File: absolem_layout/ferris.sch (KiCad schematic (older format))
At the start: 109 parts, among them IC1 NUF2221W1T2G, J1 USB C, K0_0 KEYSW, K0_1 KEYSW, K0_2 KEYSW, K0_3 KEYSW, K0_4 KEYSW, K0_5 KEYSW, K0_6 KEYSW, K0_7 KEYSW, K0_8 KEYSW, K0_9 KEYSW, K1_0 KEYSW, K1_1 KEYSW, K1_2 KEYSW, K1_3 KEYSW, K1_4 KEYSW, K1_5 KEYSW, K1_6 KEYSW, K1_7 KEYSW, K1_8 KEYSW, K1_9 KEYSW, K2_0 KEYSW, K2_1 KEYSW, K2_2 KEYSW, K2_3 KEYSW, K2_4 KEYSW, K2_5 KEYSW, K2_6 KEYSW, K2_7 KEYSW, K2_8 KEYSW, K2_9 KEYSW, K3_2 KEYSW, K3_3 KEYSW, K3_4 KEYSW, K3_5 KEYSW, K3_6 KEYSW, K3_7 KEYSW, SW1 SW_PUSH, SW2 SW_PUSH, U1 ATmega32U4-AU, U2 TLV70012_SOT23-5, U3 STM32F303CBTx, Y1 Crystal, Y2 8MHz

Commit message: More connections, removed line termination resistors (now we use an IC for it!)
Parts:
- removed C1, C2: 22p, Capacitor_SMD:C_0805_2012Metric_Pad1.15x1.40mm_HandSolder, symbol ferris-rescue:C_Small-Device
- removed C3, C4, C5, C6: 0.1u, Capacitor_SMD:C_0805_2012Metric_Pad1.15x1.40mm_HandSolder, symbol ferris-rescue:C_Small-Device
- removed C7: 4.7u, Capacitor_SMD:C_0805_2012Metric_Pad1.15x1.40mm_HandSolder, symbol ferris-rescue:C_Small-Device
- removed C8: 1u, Capacitor_SMD:C_0805_2012Metric_Pad1.15x1.40mm_HandSolder, symbol ferris-rescue:C_Small-Device
- removed R1, R2: 10k, Resistor_SMD:R_0805_2012Metric_Pad1.15x1.40mm_HandSolder, symbol ferris-rescue:R-Device
- removed R3, R4: 22, Resistor_SMD:R_0805_2012Metric_Pad1.15x1.40mm_HandSolder, symbol ferris-rescue:R-Device
- removed SW1: SW_PUSH, Button_Switch_SMD:SW_SPST_B3U-1000P, symbol ferris-rescue:SW_PUSH-keyboard_parts-ferris-rescue
- removed U1: ATmega32U4-AU, Package_QFP:TQFP-44_10x10mm_P0.8mm, symbol ferris-rescue:ATmega32U4-AU-MCU_Microchip_ATmega
- removed Y1: Crystal, Crystal:Crystal_SMD_3225-4Pin_3.2x2.5mm, symbol ferris-rescue:Crystal_GND24_Small-Device
- added J2: Conn_01x05_Male, Connector_PinHeader_2.54mm:PinHeader_1x05_P2.54mm_Vertical, symbol Connector:Conn_01x05_Male
- gave numbers to parts that had none: 6
- renumbered C9 to C1, C12 to C10, C13 to C11, C10 to C2, C11 to C6, D0_0 to D0_1, D0_9 to D0_10, D0_1 to D0_2, D0_2 to D0_3, D0_3 to D0_4, D0_4 to D0_5, D0_5 to D0_6, D0_6 to D0_7, D0_7 to D0_8, D0_8 to D0_9, D1_0 to D1_1, D1_9 to D1_10, D1_1 to D1_2, D1_2 to D1_3, D1_3 to D1_4, D1_4 to D1_5, D1_5 to D1_6, D1_6 to D1_7, D1_7 to D1_8, D1_8 to D1_9, D2_0 to D2_1, D2_9 to D2_10, D2_1 to D2_2, D2_2 to D2_3, D2_3 to D2_4, D2_4 to D2_5, D2_5 to D2_6, D2_6 to D2_7, D2_7 to D2_8, D2_8 to D2_9, D3_2 to D3_1, D3_3 to D3_2, D3_4 to D3_3, D3_5 to D3_4, D3_6 to D3_5, D3_7 to D3_6, K0_0 to K0_1, K0_9 to K0_10, K0_1 to K0_2, K0_2 to K0_3, K0_3 to K0_4, K0_4 to K0_5, K0_5 to K0_6, K0_6 to K0_7, K0_7 to K0_8, K0_8 to K0_9, K1_0 to K1_1, K1_9 to K1_10, K1_1 to K1_2, K1_2 to K1_3, K1_3 to K1_4, K1_4 to K1_5, K1_5 to K1_6, K1_6 to K1_7, K1_7 to K1_8, K1_8 to K1_9, K2_0 to K2_1, K2_9 to K2_10, K2_1 to K2_2, K2_2 to K2_3, K2_3 to K2_4, K2_4 to K2_5, K2_5 to K2_6, K2_6 to K2_7, K2_7 to K2_8, K2_8 to K2_9, K3_2 to K3_1, K3_3 to K3_2, K3_4 to K3_3, K3_5 to K3_4, K3_6 to K3_5, K3_7 to K3_6, R5 to R1, R6 to R2, R7 to R5, SW2 to SW1, U2 to U1, U3 to U2, Y2 to Y1
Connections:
- net +3V3: now also J2.5 (Pin_5)
- net D+I: now also J1.A6 (D+), J1.B6 (D+)
- net D-I: now also J1.A7 (D-), J1.B7 (D-)
- net GND: now also J2.2 (Pin_2)
- net col0: now also U2.30 (PA9)
- net col1: now also U2.29 (PA8)
- net col2: now also U2.28 (PB15)
- net col3: now also U2.27 (PB14)
- net col4: now also U2.26 (PB13)
- net col5: now also U2.31 (PA10)
- net col6: now also U2.46 (PB9)
- net col7: now also U2.42 (PB6)
- net col8: now also U2.41 (PB5)
- net col9: now also U2.40 (PB4)
- net row0: now also U2.16 (PA6)
- net row1: now also U2.15 (PA5)
- net row2: now also U2.14 (PA4)
- net row3: now also U2.13 (PA3)
- net LAYER_LED: now reaches D1.4 (DIN)
- net SWD_IO: now reaches U2.34 (PA13)
- net SWD_IO: now also J2.1 (Pin_1)
- net SWCLK: now reaches U2.37 (PA14)
- net SWCLK: now also J2.3 (Pin_3)
- net NRST: now reaches C11.1, U2.7 (NRST)
- net NRST: now also J2.4 (Pin_4)
- no-connect marks 16 -> 3

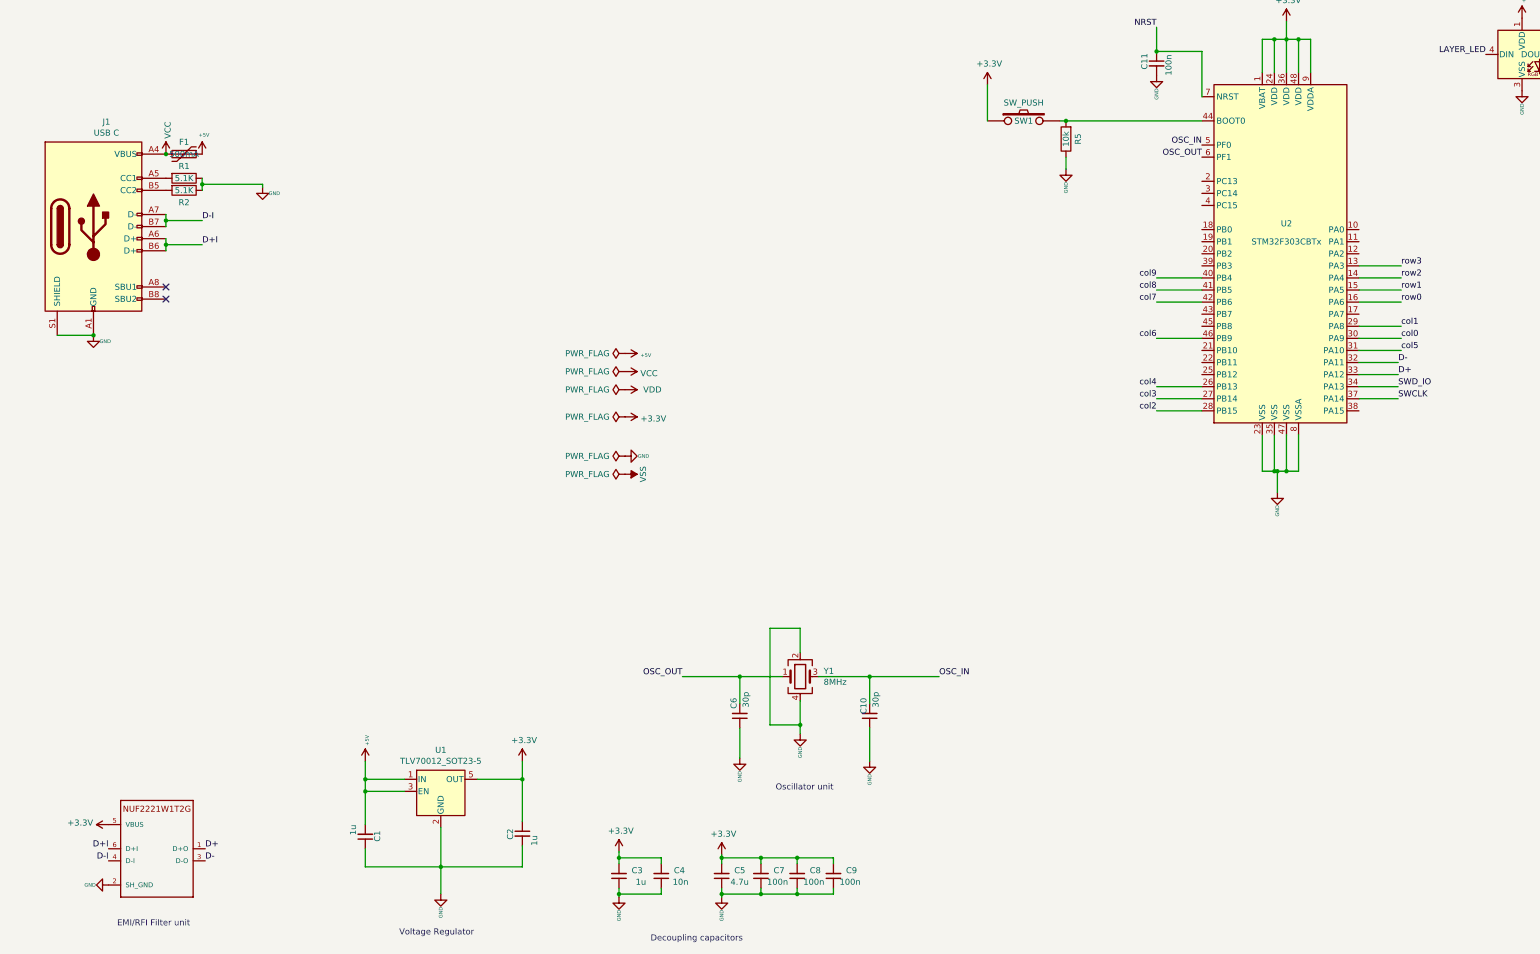
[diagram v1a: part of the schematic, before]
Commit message: Connected up most of the power. PCB incomplete still
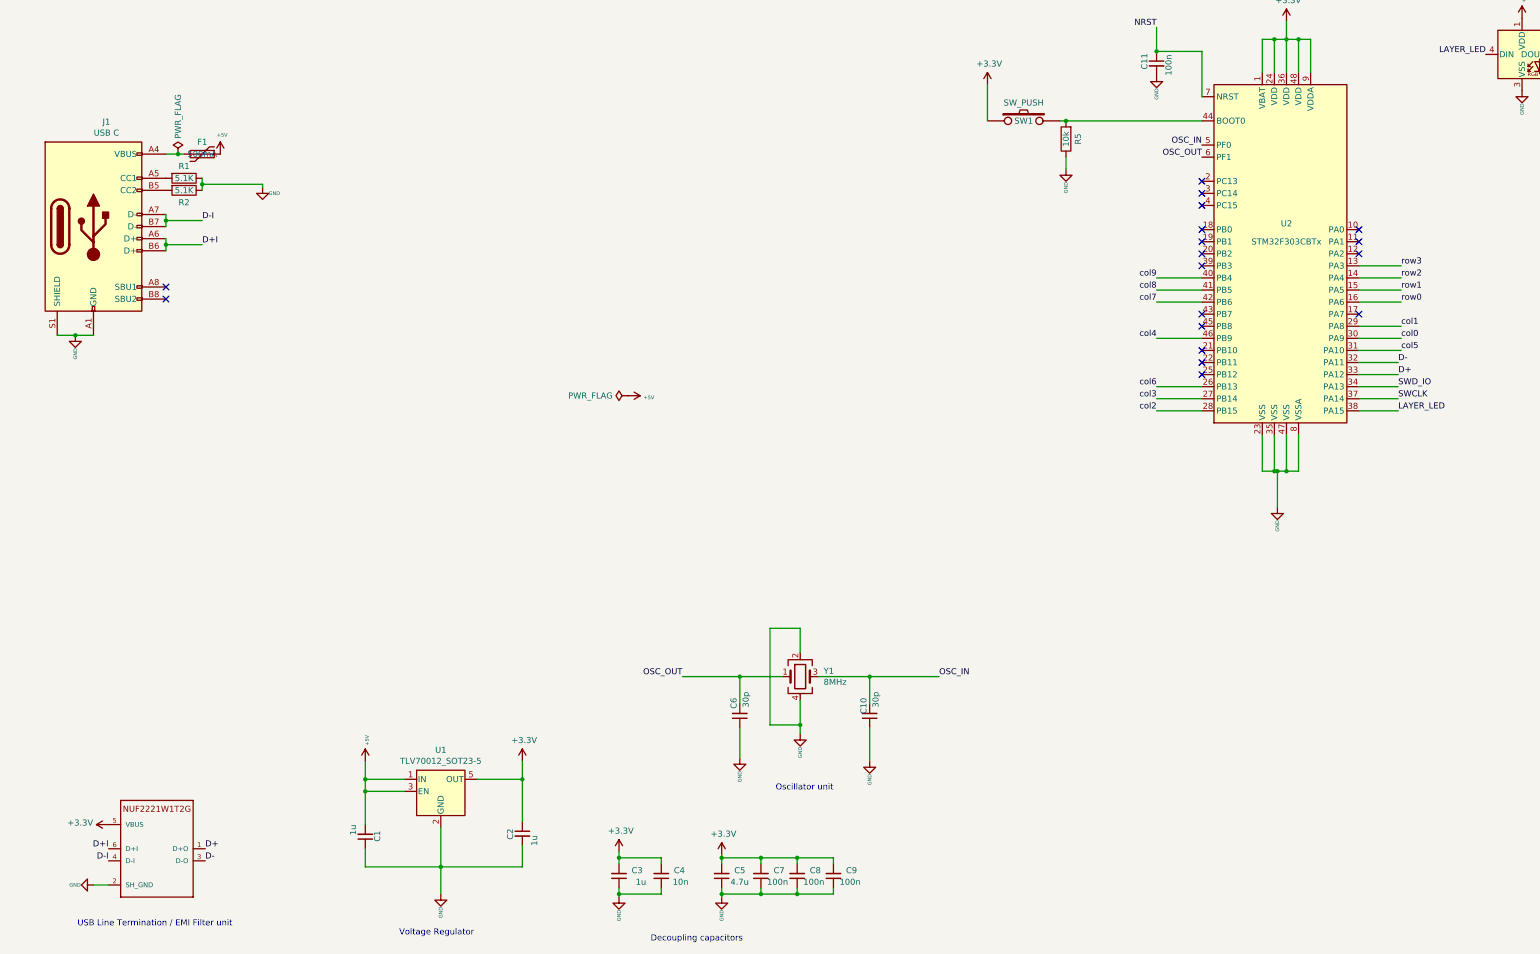
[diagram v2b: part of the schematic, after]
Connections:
- net LAYER_LED: now also U2.38 (PA15)
- net col4: now also U2.46 (PB9); no longer U2.26 (PB13)
- net col6: now also U2.26 (PB13); no longer U2.46 (PB9)
- net VCC: no longer names the net of F1.2, J1.A4 (VBUS), J1.A9 (VBUS), J1.B4 (VBUS), J1.B9 (VBUS)
- no-connect marks 3 -> 19
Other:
- note added: "USB Line Termination / EMI Filter unit"
- note removed: "EMI/RFI Filter unit"
- moved on the sheet: F1

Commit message: Updated the routing and positons
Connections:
- net col0: now also U2.41 (PB5); no longer U2.30 (PA9)
- net col1: now also U2.40 (PB4); no longer U2.29 (PA8)
- net col2: now also U2.42 (PB6); no longer U2.28 (PB15)
- net col3: now also U2.43 (PB7); no longer U2.27 (PB14)
- net col5: now also U2.14 (PA4); no longer U2.31 (PA10)
- net col6: now also U2.15 (PA5); no longer U2.26 (PB13)
- net col7: now also U2.16 (PA6); no longer U2.42 (PB6)
- net col8: now also U2.28 (PB15); no longer U2.41 (PB5)
- net col9: now also U2.27 (PB14); no longer U2.40 (PB4)
- net row0: now also U2.31 (PA10); no longer U2.16 (PA6)
- net row1: now also U2.30 (PA9); no longer U2.15 (PA5)
- net row2: now also U2.29 (PA8); no longer U2.14 (PA4)
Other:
- note added: "USB Connection"
- moved on the sheet: F1, J1, R1, R2
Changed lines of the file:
@@
 L ferris-rescue:R-Device R1
 U 1 1 5ED68FE1
-P 1700 4800
-F 0 "R1" V 1600 4800 50  0000 C CNN
-F 1 "5.1K" V 1700 4800 50  0000 C CNN
-F 2 "Resistor_SMD:R_0805_2012Metric_Pad1.15x1.40mm_HandSolder" V 1630 4800 50  0001 C CNN
-F 3 "~" H 1700 4800 50  0001 C CNN
-F 4 "C27834" V 1700 4800 50  0001 C CNN "LCSC Part #"
-	1    1700 4800
+P 2550 4975
+F 0 "R1" V 2450 4975 50  0000 C CNN
+F 1 "5.1K" V 2550 4975 50  0000 C CNN
+F 2 "Resistor_SMD:R_0805_2012Metric_Pad1.15x1.40mm_HandSolder" V 2480 4975 50  0001 C CNN
+F 3 "~" H 2550 4975 50  0001 C CNN
+F 4 "C27834" V 2550 4975 50  0001 C CNN "LCSC Part #"
+	1    2550 4975
 	0    1    1    0
 $EndComp
@@
 L ferris-rescue:R-Device R2
 U 1 1 5ED69FD6
-P 1700 4900
-F 0 "R2" V 1800 4900 50  0000 C CNN
-F 1 "5.1K" V 1700 4900 50  0000 C CNN
-F 2 "Resistor_SMD:R_0805_2012Metric_Pad1.15x1.40mm_HandSolder" V 1630 4900 50  0001 C CNN
-F 3 "~" H 1700 4900 50  0001 C CNN
-	1    1700 4900
+P 2550 5075
+F 0 "R2" V 2650 5075 50  0000 C CNN
+F 1 "5.1K" V 2550 5075 50  0000 C CNN
+F 2 "Resistor_SMD:R_0805_2012Metric_Pad1.15x1.40mm_HandSolder" V 2480 5075 50  0001 C CNN
+F 3 "~" H 2550 5075 50  0001 C CNN
+	1    2550 5075
 	0    1    1    0
 $EndComp
@@
 L power:GND #PWR06
 U 1 1 5ED72D47
-P 2350 4875
-F 0 "#PWR06" H 2350 4925 20  0001 C CNN
-F 1 "GND" H 2400 4825 30  0000 L CNN
-F 2 "" H 2350 4875 60  0000 C CNN
-F 3 "" H 2350 4875 60  0000 C CNN
-	1    2350 4875
-	1    0    0    -1
-$EndComp
-Wire Wire Line
-	1550 5400 1550 5350
-Wire Wire Line
-	1550 5200 1550 5150
+P 3200 5050
+F 0 "#PWR06" H 3200 5100 20  0001 C CNN
+F 1 "GND" H 3250 5000 30  0000 L CNN
+F 2 "" H 3200 5050 60  0000 C CNN
+F 3 "" H 3200 5050 60  0000 C CNN
+	1    3200 5050
+	1    0    0    -1
+$EndComp
+Wire Wire Line
+	2400 5575 2400 5525
+Wire Wire Line
+	2400 5375 2400 5325
 $Comp
 L ferris-rescue:USB_C_Receptacle_USB2.0-Connector J1
 U 1 1 5EF5D00C
-P 950 5200
-F 0 "J1" H 1057 6067 50  0000 C CNN
-F 1 "USB C" H 1057 5976 50  0000 C CNN
-F 2 "Connector_USB:USB_C_Receptacle_HRO_TYPE-C-31-M-12" H 1100 5200 50  0001 C CNN
-F 3 "https://www.usb.org/sites/default/files/documents/usb_type-c.zip" H 1100 5200 50  0001 C CNN
-F 4 "C165948" H 950 5200 50  0001 C CNN "LCSC Part #"
-	1    950  5200
+P 1800 5375
+F 0 "J1" H 1907 6242 50  0000 C CNN
+F 1 "USB C" H 1907 6151 50  0000 C CNN
+F 2 "Connector_USB:USB_C_Receptacle_HRO_TYPE-C-31-M-12" H 1950 5375 50  0001 C CNN
+F 3 "https://www.usb.org/sites/default/files/documents/usb_type-c.zip" H 1950 5375 50  0001 C CNN
+F 4 "C165948" H 1800 5375 50  0001 C CNN "LCSC Part #"
+	1    1800 5375
 	1    0    0    -1
 $EndComp
@@
 Wire Wire Line
 	7750 900  7750 1200
-Text Label 15200 875  2    50   ~ 0
-row1,0
-Text Label 15200 1000 2    50   ~ 0
-row1,1
 $Comp
 L ferris-rescue:KEYSW-keyboard_parts-ferris-rescue K1_6
@@
 	1    0    0    -1
 $EndComp
-Text Label 15200 1125 2    50   ~ 0
-row1,2
 $Comp
 L ferris-rescue:D-Device D2_6
@@
 Wire Wire Line
 	8550 2700 9250 2700
-NoConn ~ 1550 5700
-NoConn ~ 1550 5800
+NoConn ~ 2400 5875
+NoConn ~ 2400 5975
 Wire Wire Line
 	10550 1800 10550 2400
@@
 Connection ~ 7750 2400
 Connection ~ 7150 3300
-Text Label 1850 5350 0    50   ~ 0
+Text Label 2700 5525 0    50   ~ 0
 D+I
-Text Label 1850 5150 0    50   ~ 0
+Text Label 2700 5325 0    50   ~ 0
 D-I
 $Comp
 L ferris-rescue:Polyfuse-Device F1
 U 1 1 5EF6C20F
-P 1850 4600
-F 0 "F1" V 1750 4600 50  0000 C CNN
-F 1 "500mA" V 1850 4600 50  0000 C CNN
-F 2 "Fuse:Fuse_1206_3216Metric" H 1900 4400 50  0001 L CNN
-F 3 "~" H 1850 4600 50  0001 C CNN
-F 4 "C151162" V 1850 4600 50  0001 C CNN "LCSC Part #"
-	1    1850 4600
+P 2700 4775
+F 0 "F1" V 2600 4775 50  0000 C CNN
+F 1 "500mA" V 2700 4775 50  0000 C CNN
+F 2 "Fuse:Fuse_1206_3216Metric" H 2750 4575 50  0001 L CNN
+F 3 "~" H 2700 4775 50  0001 C CNN
+F 4 "C151162" V 2700 4775 50  0001 C CNN "LCSC Part #"
+	1    2700 4775
 	0    1    1    0
 $EndComp
@@
 L ferris-rescue:+5V-power #PWR05
 U 1 1 5EF7A4D9
-P 2000 4600
-F 0 "#PWR05" H 2000 4570 20  0001 C CNN
-F 1 "+5V" H 2015 4758 30  0000 C CNN
-F 2 "" H 2000 4600 60  0000 C CNN
-F 3 "" H 2000 4600 60  0000 C CNN
-	1    2000 4600
-	1    0    0    -1
-$EndComp
-Wire Wire Line
-	1850 4800 1850 4850
-Wire Wire Line
-	650  6100 800  6100
+P 2850 4775
+F 0 "#PWR05" H 2850 4745 20  0001 C CNN
+F 1 "+5V" H 2865 4933 30  0000 C CNN
+F 2 "" H 2850 4775 60  0000 C CNN
+F 3 "" H 2850 4775 60  0000 C CNN
+	1    2850 4775
+	1    0    0    -1
+$EndComp
+Wire Wire Line
+	2700 4975 2700 5025
+Wire Wire Line
+	1500 6275 1650 6275
 $Comp
 L ferris-rescue:+5V-power #PWR012
@@
 	7850 3300 8550 3300
 Connection ~ 7850 3300
-Text Label 15200 1250 2    50   ~ 0
-row1,3
 Wire Wire Line
 	3850 2700 7150 2700
@@
 Connection ~ 4450 2400
 NoConn ~ 13075 3775
-Text Label 15500 1250 0    50   ~ 0
-row1,3
-Text Label 15525 1100 0    50   ~ 0
-row1,2
-Text Label 15500 975  0    50   ~ 0
-row1,1
-Text Label 15525 850  0    50   ~ 0
-row1,0
 $Comp
 L NUF2221W1T2G:NUF2221W1T2G IC1
@@
 Wire Wire Line
 	11425 5825 11775 5825
-Text Label 11775 5625 0    50   ~ 0
+Text Label 11775 6025 0    50   ~ 0
 row2
-Text Label 11775 5725 0    50   ~ 0
+Text Label 11775 6125 0    50   ~ 0
 row1
+Text Label 11775 6225 0    50   ~ 0
+row0
+Wire Wire Line
+	11425 6025 11775 6025
+Wire Wire Line
+	11425 6125 11775 6125
+Wire Wire Line
+	11425 6225 11775 6225
 Text Label 11775 5825 0    50   ~ 0
-row0
-Wire Wire Line
-	11425 6025 11775 6025
-Wire Wire Line
-	11425 6125 11775 6125
-Wire Wire Line
-	11425 6225 11775 6225
-Text Label 11775 6025 0    50   ~ 0
-col1
-Text Label 11775 6125 0    50   ~ 0
+col7
+Text Label 9750 5725 2    50   ~ 0
 col0
-Text Label 11775 6225 0    50   ~ 0
-col5
 $Comp
 L ferris-rescue:WS2812B-LED D1
@@
 Text Label 12475 3775 2    50   ~ 0
 LAYER_LED
-Text Label 9750 6725 2    50   ~ 0
-col2
 Wire Wire Line
 	9750 6725 10125 6725
@@
 	10125 6625 9750 6625
 Wire Wire Line
-	10125 6525 9750 6525
-Wire Wire Line
 	10125 6125 9750 6125
-Text Label 9750 6625 2    50   ~ 0
-col3
 Text Label 9750 6125 2    50   ~ 0
 col4
-Text Label 9750 6525 2    50   ~ 0
+Text Label 11775 5725 0    50   ~ 0
 col6
-Text Label 9750 5825 2    50   ~ 0
-col7
+Text Label 9750 5625 2    50   ~ 0
+col1
 Wire Wire Line
 	9750 5825 10125 5825
@@
 Wire Wire Line
 	10125 5625 9750 5625
-Text Label 9750 5725 2    50   ~ 0
+Text Label 9750 6725 2    50   ~ 0
 col8
-Text Label 9750 5625 2    50   ~ 0
+Text Label 9750 6625 2    50   ~ 0
 col9
 Text Label 9750 3550 2    50   ~ 0
@@
 	11750 6625 11425 6625
 Wire Wire Line
-	1550 5150 1850 5150
-Connection ~ 1550 5150
-Wire Wire Line
-	1550 5150 1550 5100
-Wire Wire Line
-	1850 5350 1550 5350
-Connection ~ 1550 5350
-Wire Wire Line
-	1550 5350 1550 5300
-Wire Wire Line
-	1850 4850 2350 4850
-Wire Wire Line
-	2350 4850 2350 4875
-Connection ~ 1850 4850
-Wire Wire Line
-	1850 4850 1850 4900
+	2400 5325 2700 5325
+Connection ~ 2400 5325
+Wire Wire Line
+	2400 5325 2400 5275
+Wire Wire Line
+	2700 5525 2400 5525
+Connection ~ 2400 5525
+Wire Wire Line
+	2400 5525 2400 5475
+Wire Wire Line
+	2700 5025 3200 5025
+Wire Wire Line
+	3200 5025 3200 5050
+Connection ~ 2700 5025
+Wire Wire Line
+	2700 5025 2700 5075
 NoConn ~ 10125 4825
 NoConn ~ 10125 4925
@@
 NoConn ~ 10125 6325
 NoConn ~ 10125 6225
-NoConn ~ 10125 5925
 NoConn ~ 10125 6025
 NoConn ~ 10125 5325
@@
 L power:GND #PWR0101
 U 1 1 5F8C4642
-P 800 6100
-F 0 "#PWR0101" H 800 6150 20  0001 C CNN
-F 1 "GND" V 800 5900 30  0000 L CNN
-F 2 "" H 800 6100 60  0000 C CNN
-F 3 "" H 800 6100 60  0000 C CNN
-	1    800  6100
-	1    0    0    -1
-$EndComp
-Connection ~ 800  6100
-Wire Wire Line
-	800  6100 950  6100
+P 1650 6275
+F 0 "#PWR0101" H 1650 6325 20  0001 C CNN
+F 1 "GND" V 1650 6075 30  0000 L CNN
+F 2 "" H 1650 6275 60  0000 C CNN
+F 3 "" H 1650 6275 60  0000 C CNN
+	1    1650 6275
+	1    0    0    -1
+$EndComp
+Connection ~ 1650 6275
+Wire Wire Line
+	1650 6275 1800 6275
 $Comp
 L power:GND #PWR0102
@@
 $EndComp
 Wire Wire Line
-	1700 4600 1650 4600
+	2550 4775 2500 4775
 Wire Wire Line
 	1075 10650 950  10650
@@
 L ferris-rescue:PWR_FLAG-power #FLG0102
 U 1 1 5F962B5E
-P 1650 4600
-F 0 "#FLG0102" H 1650 4675 50  0001 C CNN
-F 1 "PWR_FLAG" V 1650 4727 50  0000 L CNN
-F 2 "" H 1650 4600 50  0001 C CNN
-F 3 "~" H 1650 4600 50  0001 C CNN
-	1    1650 4600
-	1    0    0    -1
-$EndComp
-Connection ~ 1650 4600
-Wire Wire Line
-	1650 4600 1550 4600
+P 2500 4775
+F 0 "#FLG0102" H 2500 4850 50  0001 C CNN
+F 1 "PWR_FLAG" V 2500 4902 50  0000 L CNN
+F 2 "" H 2500 4775 50  0001 C CNN
+F 3 "~" H 2500 4775 50  0001 C CNN
+	1    2500 4775
+	1    0    0    -1
+$EndComp
+Connection ~ 2500 4775
+Wire Wire Line
+	2500 4775 2400 4775
 Text Label 11750 6725 0    50   ~ 0
 LAYER_LED
 Wire Wire Line
 	11750 6725 11425 6725
+Wire Wire Line
+	10125 5925 9750 5925
+Text Label 9750 5825 2    50   ~ 0
+col2
+Text Label 9750 5925 2    50   ~ 0
+col3
+Text Label 11775 5625 0    50   ~ 0
+col5
+NoConn ~ 10125 6525
+Text Notes 2025 6650 2    50   ~ 0
+USB Connection
 $EndSCHEMATC

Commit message: Prefinal version
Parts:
- removed J2: Conn_01x05_Male, Connector_PinHeader_2.54mm:PinHeader_1x05_P2.54mm_Vertical, symbol Connector:Conn_01x05_Male
- added C12: 10uF, Capacitor_SMD:C_0805_2012Metric_Pad1.15x1.40mm_HandSolder, symbol ferris-rescue:C_Small-Device
- added D1_11: D, Diode_SMD:D_SOD-123, symbol ferris-rescue:D-Device
- added Q1: DTC123J, Package_TO_SOT_SMD:SOT-23, symbol Transistor_BJT:DTC123J
- C11: value 100n -> 4.7nF
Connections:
- net GND: now also C12.2, Q1.2 (E)
- net at R5.2, U2.44 (BOOT0): now also C12.1, D1_11.1 (K); no longer SW1.2
- net NRST: no longer names the net of C11.1, U2.7 (NRST)
- net NRST: now also Q1.3 (C)
- new net: D1_11.2 (A), Q1.1 (B), SW1.2
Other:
- moved on the sheet: C1, C10, C11, C2, C3, C4, C5, C6, C7, C8, C9, D1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
